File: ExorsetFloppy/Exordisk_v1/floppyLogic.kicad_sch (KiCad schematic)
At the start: 92 parts, among them J10 Conn_01x01, J11 Conn_01x01, J12 Conn_01x01, J13 Conn_01x01, J14 Conn_01x01, J15 Conn_01x01, J16 Conn_01x01, J17 Conn_01x01, J18 Conn_01x01, J19 Conn_02x02_Odd_Even, J2 Floppy, J20 Conn_01x01, J21 Conn_01x01, J22 Conn_01x01, J23 Conn_01x01, J24 Conn_01x01, J25 Conn_01x01, J26 Conn_01x01, J27 Conn_01x01, J28 Conn_01x01, J29 Conn_01x01, J3 Conn_01x01, J30 Conn_01x01, J31 Conn_01x01, J32 Conn_01x01, J33 Conn_01x01, J34 Conn_01x01, J35 Conn_01x01, J36 Conn_01x01, J37 Conn_01x01, J38 Conn_01x01, J39 Conn_01x01, J40 Conn_01x01, J41 Conn_01x01, J42 Conn_01x01, J43 Conn_01x01, J7 Conn_01x17, J8 Conn_01x01, J9 Conn_01x01, Q1 BC337, U10 GAL16V8, U11 74HCT74, U12 74HCT74, U15 74HCT04, U16 74HCT74, U17 74HCT00, U18 74HCT74, U19 74LS112, U2 74HCT74, U20 68B21, U21 MC4024, U22 74LS157, U23 74LS123, U24 74HCT164, U25 74LS04, U27 MC4044, U28 74F163, U29 74F163, U34 6852_DIL24, U4 MC8506_new, U5 74F163, U7 74HCT240, U8 74HCT244, U9 74LS138

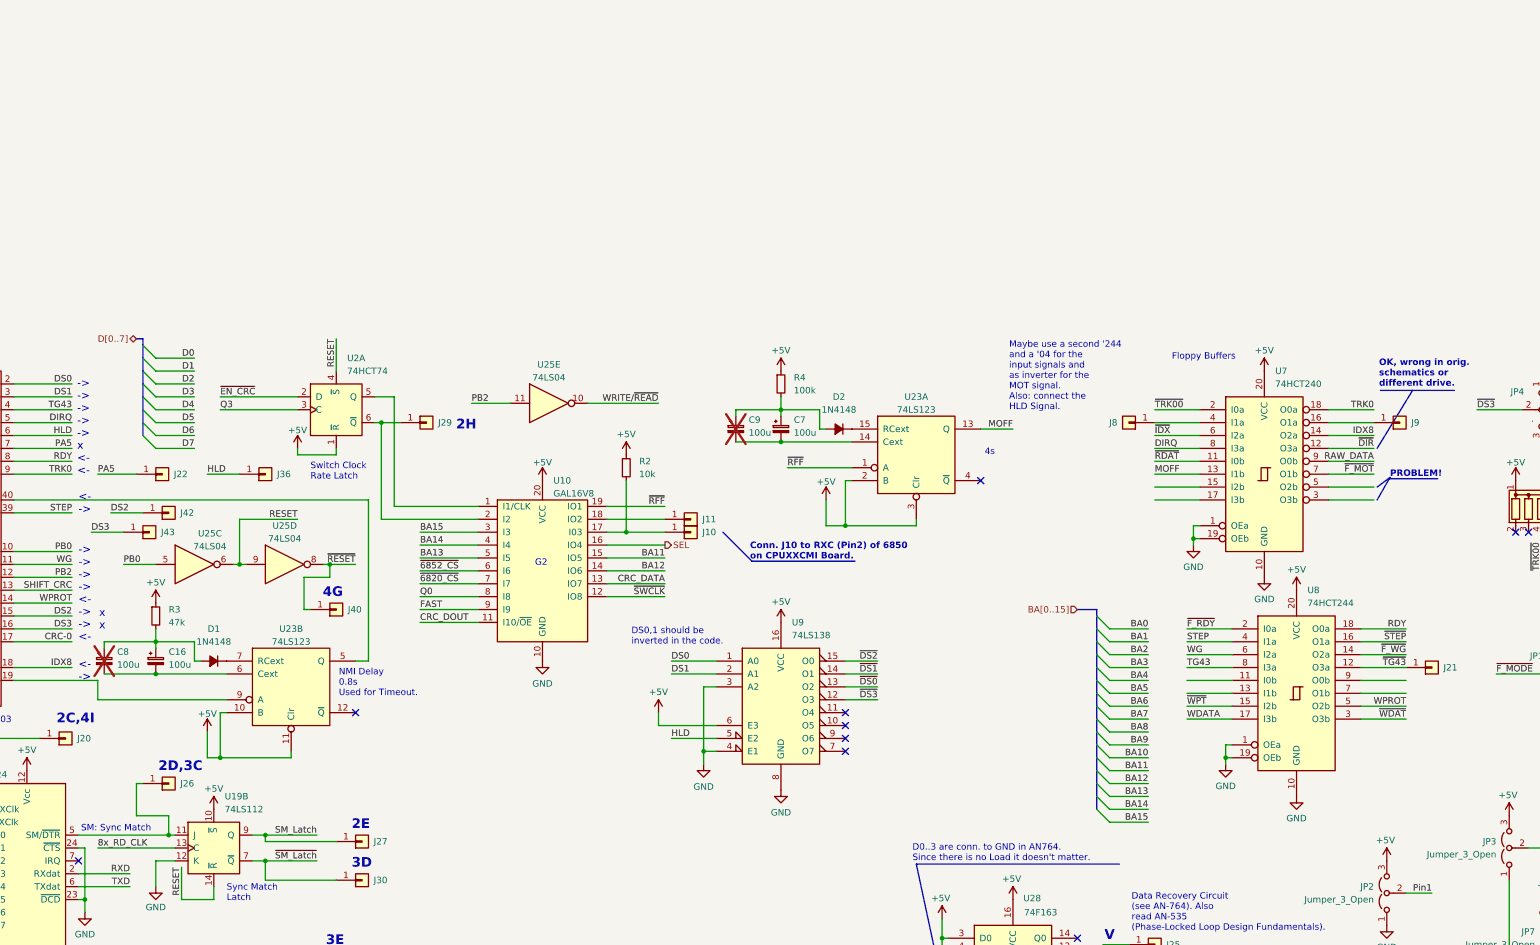
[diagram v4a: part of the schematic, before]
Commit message: new build for extra drives
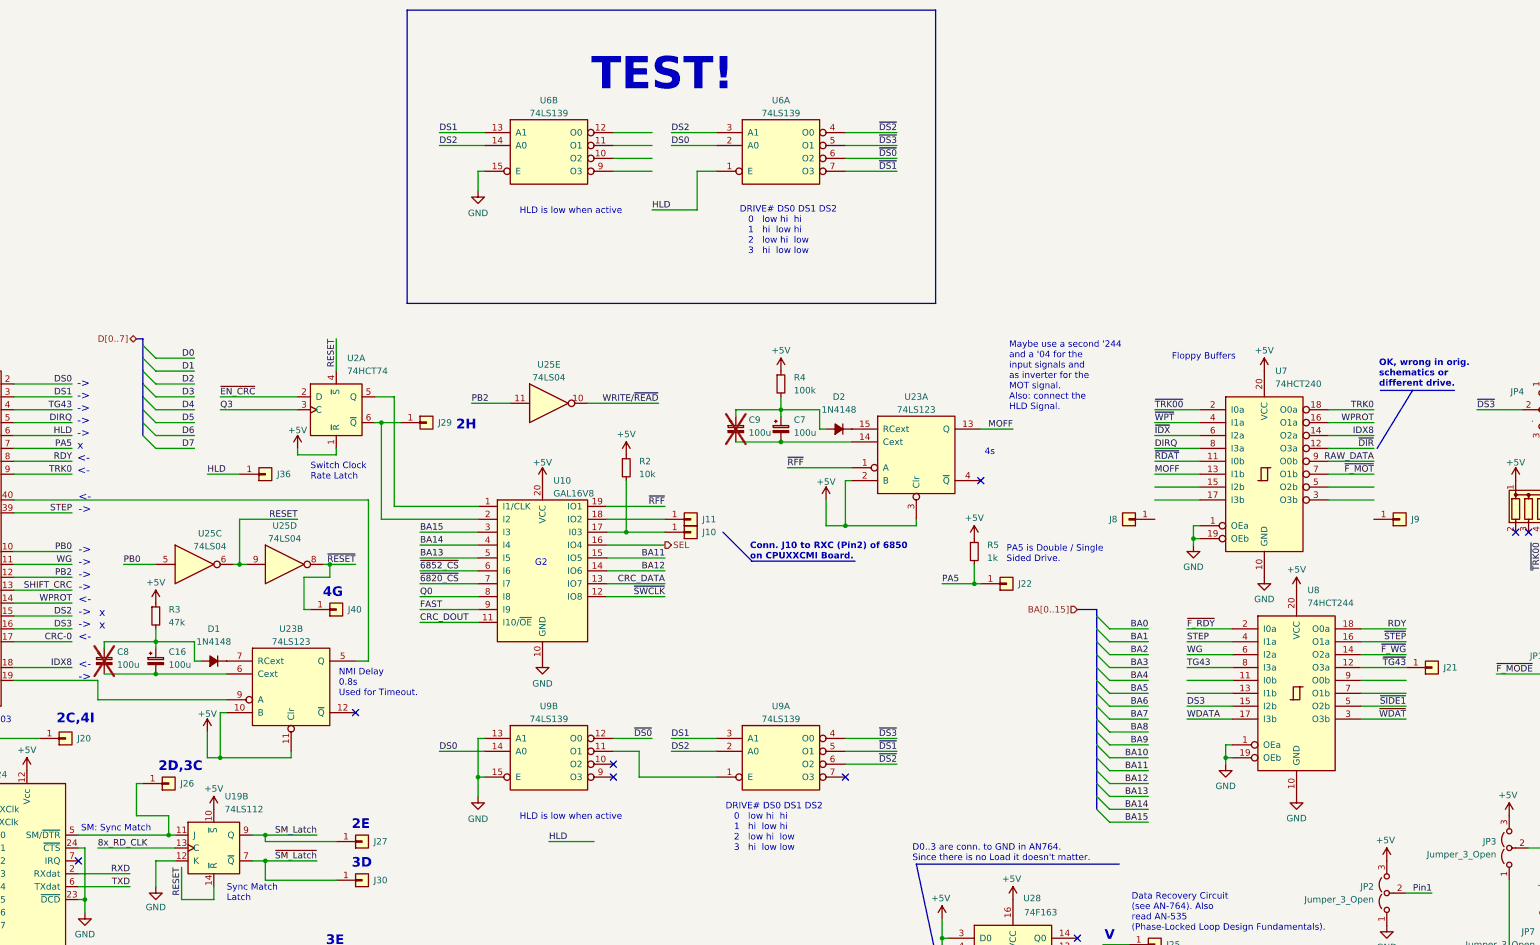
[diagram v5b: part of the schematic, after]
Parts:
- removed J42, J43: Conn_01x01, Connector_PinHeader_2.54mm:PinHeader_1x01_P2.54mm_Vertical, symbol Connector_Generic:Conn_01x01
- removed U9: 74LS138, Package_DIP:DIP-16_W7.62mm, symbol 74xx:74LS138
- added R5: 1k, Resistor_SMD:R_1206_3216Metric_Pad1.30x1.75mm_HandSolder, symbol Device:R_Small
- added U6, U9: 74LS139, Package_DIP:DIP-16_W7.62mm, symbol 74xx:74LS139
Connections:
- net +5V: now also R5.1
- net DS0: now also U6.2 (A0), U9.14 (A0)
- net DS1: now also U6.13 (A1), U9.3 (A1)
- net DS2: now also U6.14 (A0), U6.3 (A1), U9.2 (A0)
- net DS3: now also U8.15 (I2b)
- net GND: now also U6.15 (E), U9.13 (A1), U9.15 (E)
- net HLD: now also U6.1 (E)
- net PA5: now also R5.2
- net WPROT: now also U7.16 (O1a); no longer U8.5 (O2b)
- net ~{DS0}: now also U6.6 (O2), U9.12 (O0)
- net ~{DS1}: now also U6.7 (O3), U9.5 (O1)
- net ~{DS2}: now also U6.4 (O0), U9.6 (O2)
- net ~{DS3}: now also U6.5 (O1), U9.4 (O0)
- net ~{SIDE1}: now also U8.5 (O2b)
- net ~{WPT}: now also U7.4 (I1a); no longer U8.15 (I2b)
- net at J9.1 (Pin_1): no longer U7.16 (O1a)
- net at J8.1 (Pin_1): no longer U7.4 (I1a)
- new net: U9.1 (E), U9.11 (O1)
- no-connect marks 43 -> 42
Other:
- note added: "DRIVE# DS0 DS1 DS2 0 low hi hi 1 hi low hi 2 low hi low 3 hi low low"
- note added: "HLD is low when active"
- note added: "PA5 is Double / Single Sided Drive."
- note added: "TEST!"
- note removed: "DS0,1 should be inverted in the code."
- note removed: "PROBLEM!"
- moved on the sheet: J22, J8, J9

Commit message: first double sided format works
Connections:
- net HLD: no longer U6.1 (E)
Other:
- note added: "HLD is low when active, unfortunately it is high when stepping!"
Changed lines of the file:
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@@
 		)
 	)
-	(text "HLD is low when active"
+	(text "HLD is low when active,\nunfortunately it is high when stepping!"
 		(exclude_from_sim no)
-		(at 164.338 -11.176 0)
+		(at 159.766 -5.842 0)
 		(effects
 			(font
@@
 	)
 	(label "HLD"
-		(at 180.34 -11.43 0)
+		(at 179.07 -1.27 0)
 		(effects
 			(font

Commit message: Exordisk Board continued
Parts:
- removed U9: 74LS139, Package_DIP:DIP-16_W7.62mm, symbol 74xx:74LS139
- added D3, D4, D5, D6: 1N4148, Diode_SMD:D_1206_3216Metric_Pad1.42x1.75mm_HandSolder, symbol Device:D_Small_Filled
- added J42: SS/DS, Connector_PinHeader_2.54mm:PinHeader_2x04_P2.54mm_Vertical, symbol Connector_Generic:Conn_02x04_Odd_Even
- added R10, R6, R8, R9: 1k, Resistor_SMD:R_1206_3216Metric_Pad1.30x1.75mm_HandSolder, symbol Device:R_Small
- added U9: 74LS32, Package_DIP:DIP-14_W7.62mm, symbol 74xx:74LS32
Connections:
- net +5V: now also R10.1, R6.1, R8.1, R9.1
- net DS1: no longer U6.13 (A1)
- net DS2: no longer U6.14 (A0)
- net GND: now also U6.13 (A1), U6.14 (A0), J42.1 (Pin_1), J42.3 (Pin_3), J42.5 (Pin_5), J42.7 (Pin_7)
- net HLD: now also U6.1 (E)
- net PA5: now also D3.1 (K), D4.1 (K), D5.1 (K), D6.1 (K)
- net ~{DS0}: now also U9.2
- net ~{DS1}: now also U9.5
- net ~{DS2}: now also U9.10
- net ~{DS3}: now also U9.13
- new net: D5.2 (A), U9.8
- new net: D4.2 (A), U9.6
- new net: D6.2 (A), U9.11
- new net: D3.2 (A), U9.3
- new net L0: J42.2 (Pin_2), R9.2, U9.1
- new net L1: J42.4 (Pin_4), R8.2, U9.4
- new net L2: J42.6 (Pin_6), R6.2, U9.9
- new net L3: J42.8 (Pin_8), R10.2, U9.12
- no-connect marks 42 -> 43
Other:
- note added: "HLD is low when active, unfortunately it is high when stepping! This ONLY works with modified Coe!"
- note added: "not necessary with new code."
- note added: "useless."
- note removed: "HLD is low when active"
- note removed: "HLD is low when active, unfortunately it is high when stepping!"
- note removed: "TEST!"
- moved on the sheet: U6A, U6B

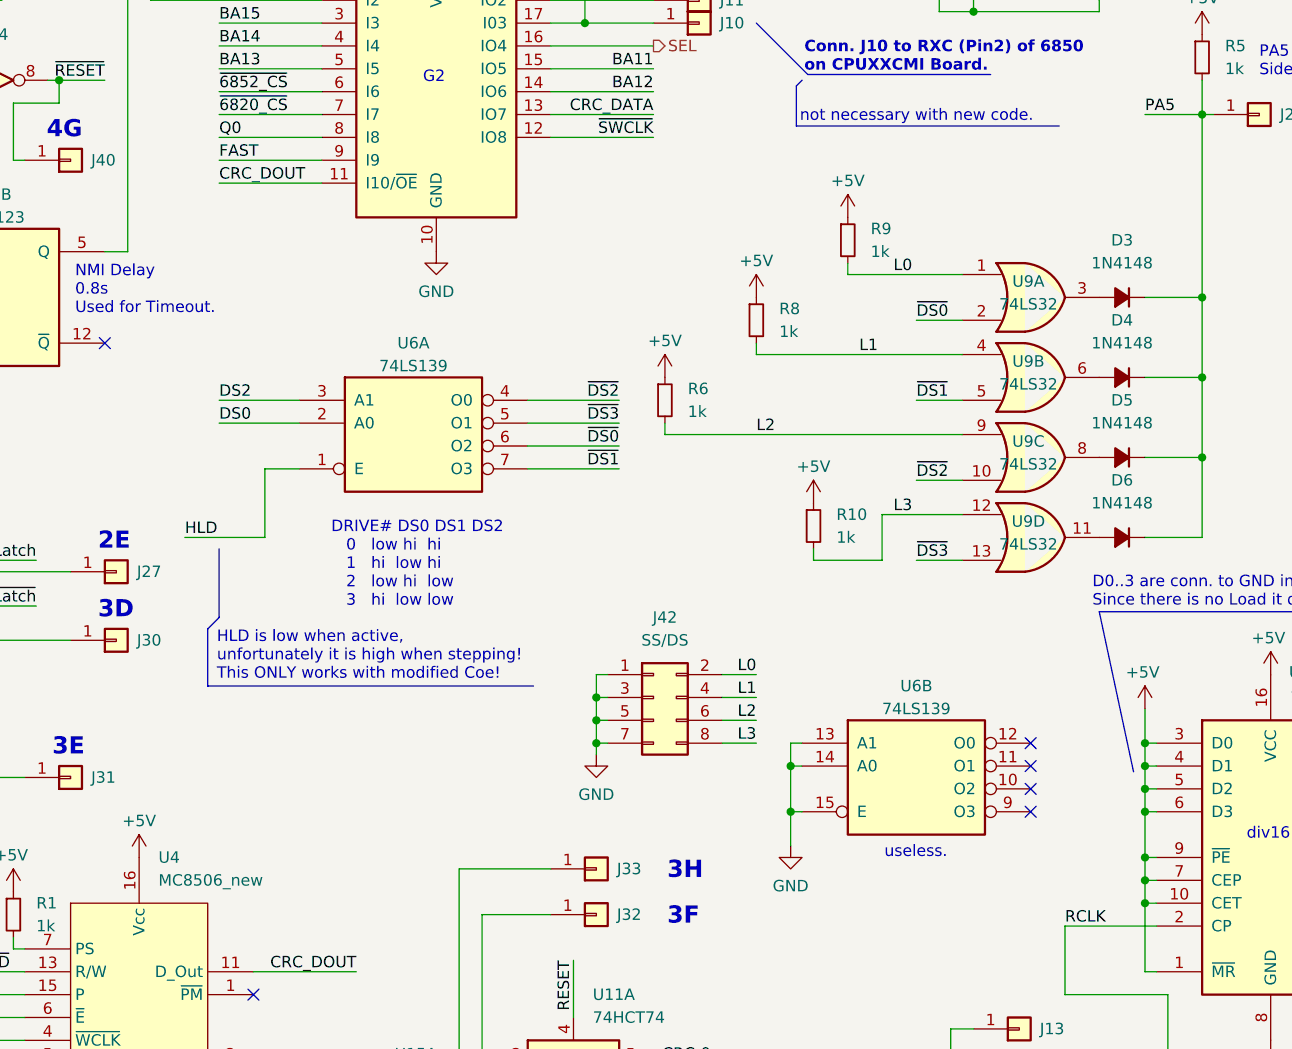
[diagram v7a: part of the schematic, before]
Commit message: exordisk firmware first working for DS
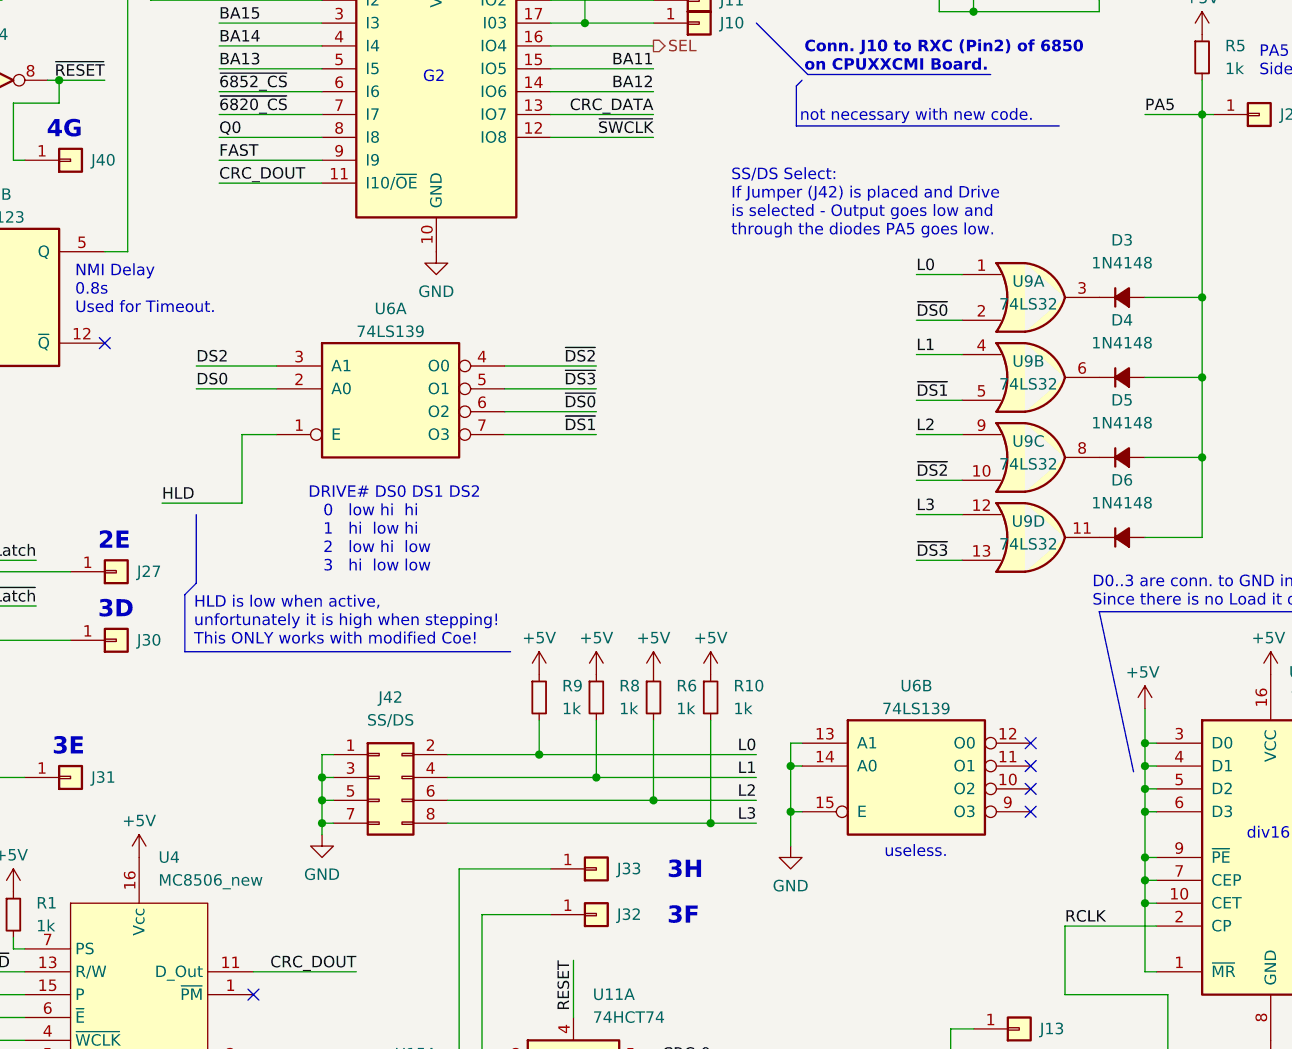
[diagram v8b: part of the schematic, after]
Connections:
- net PA5: now also D3.2 (A), D4.2 (A), D5.2 (A), D6.2 (A); no longer D3.1 (K), D4.1 (K), D5.1 (K), D6.1 (K)
- net at U9.8: now also D5.1 (K); no longer D5.2 (A)
- net at U9.6: now also D4.1 (K); no longer D4.2 (A)
- net at U9.11: now also D6.1 (K); no longer D6.2 (A)
- net at U9.3: now also D3.1 (K); no longer D3.2 (A)
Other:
- note added: "SS/DS Select: If Jumper (J42) is placed and Drive is selected - Output goes low and through the diodes PA5 goes low."
- moved on the sheet: J42, R10, R6, R8, R9, U6A
